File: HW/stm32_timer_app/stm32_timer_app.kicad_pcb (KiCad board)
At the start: 2 copper layers, 142.1 x 79.7 mm, 69 parts, among them J1 105164-0001, J2 61300411121, J3 PH2-06-UA, J4 691213710002, J5 691213710002, Q1 BTA10-600BRG, U1 RT9193-33GB, U2 MOC3041SM, U3 STM32F103C8T6, Y1 ABL-8.000MHZ-B2, Y2 ABS25-32.768KHZ-6-4-T

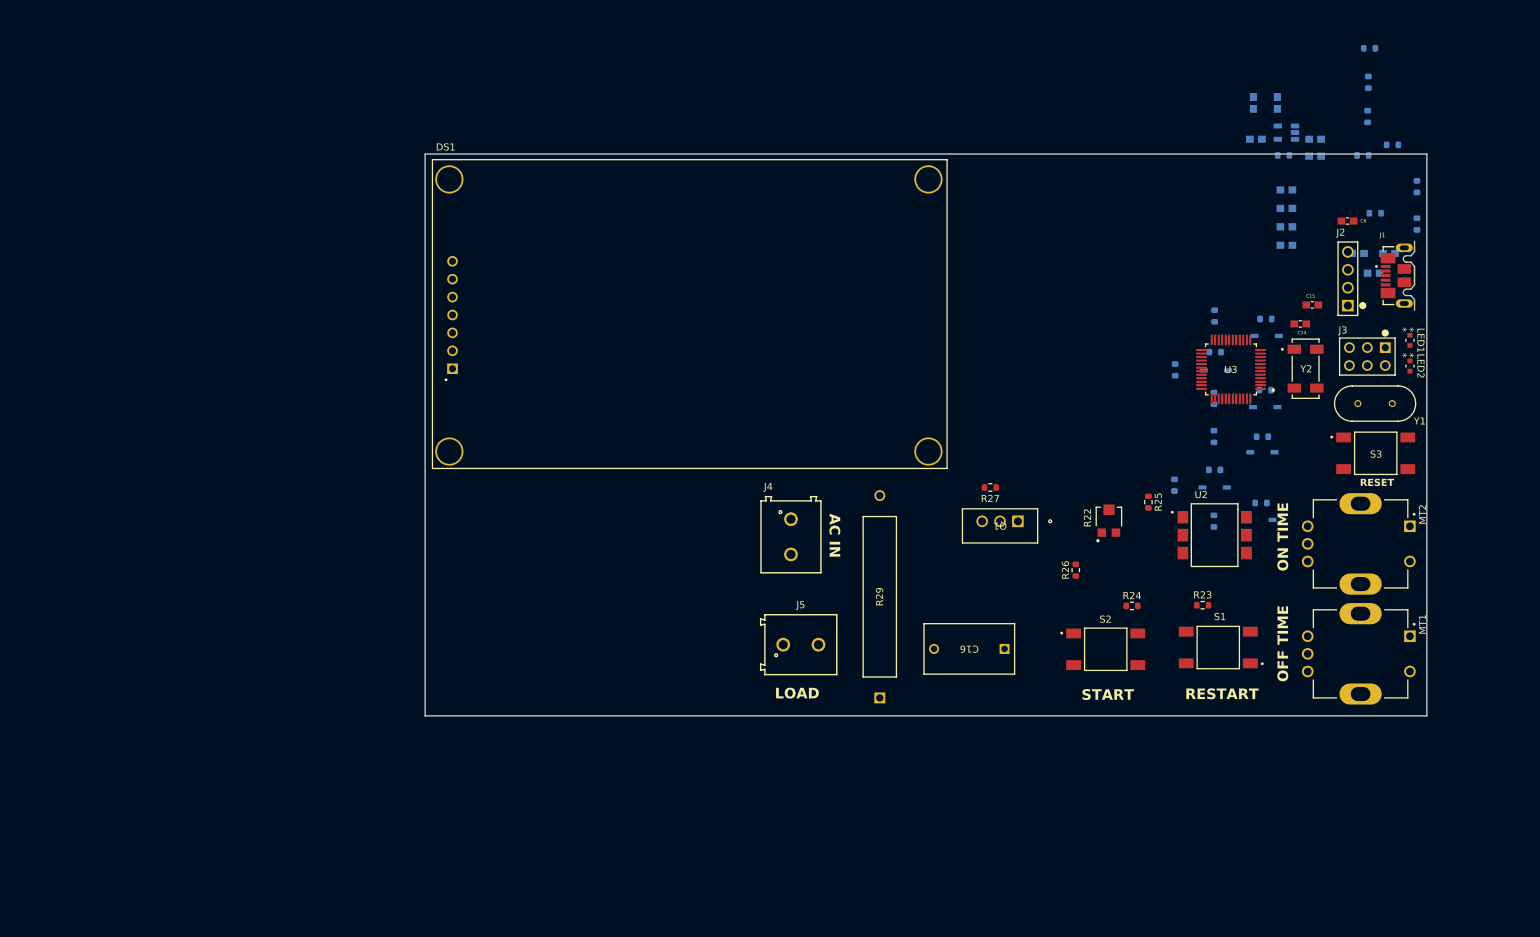
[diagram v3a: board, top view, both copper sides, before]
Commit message: update schematic
update schematic and foot print / 3D body libraries
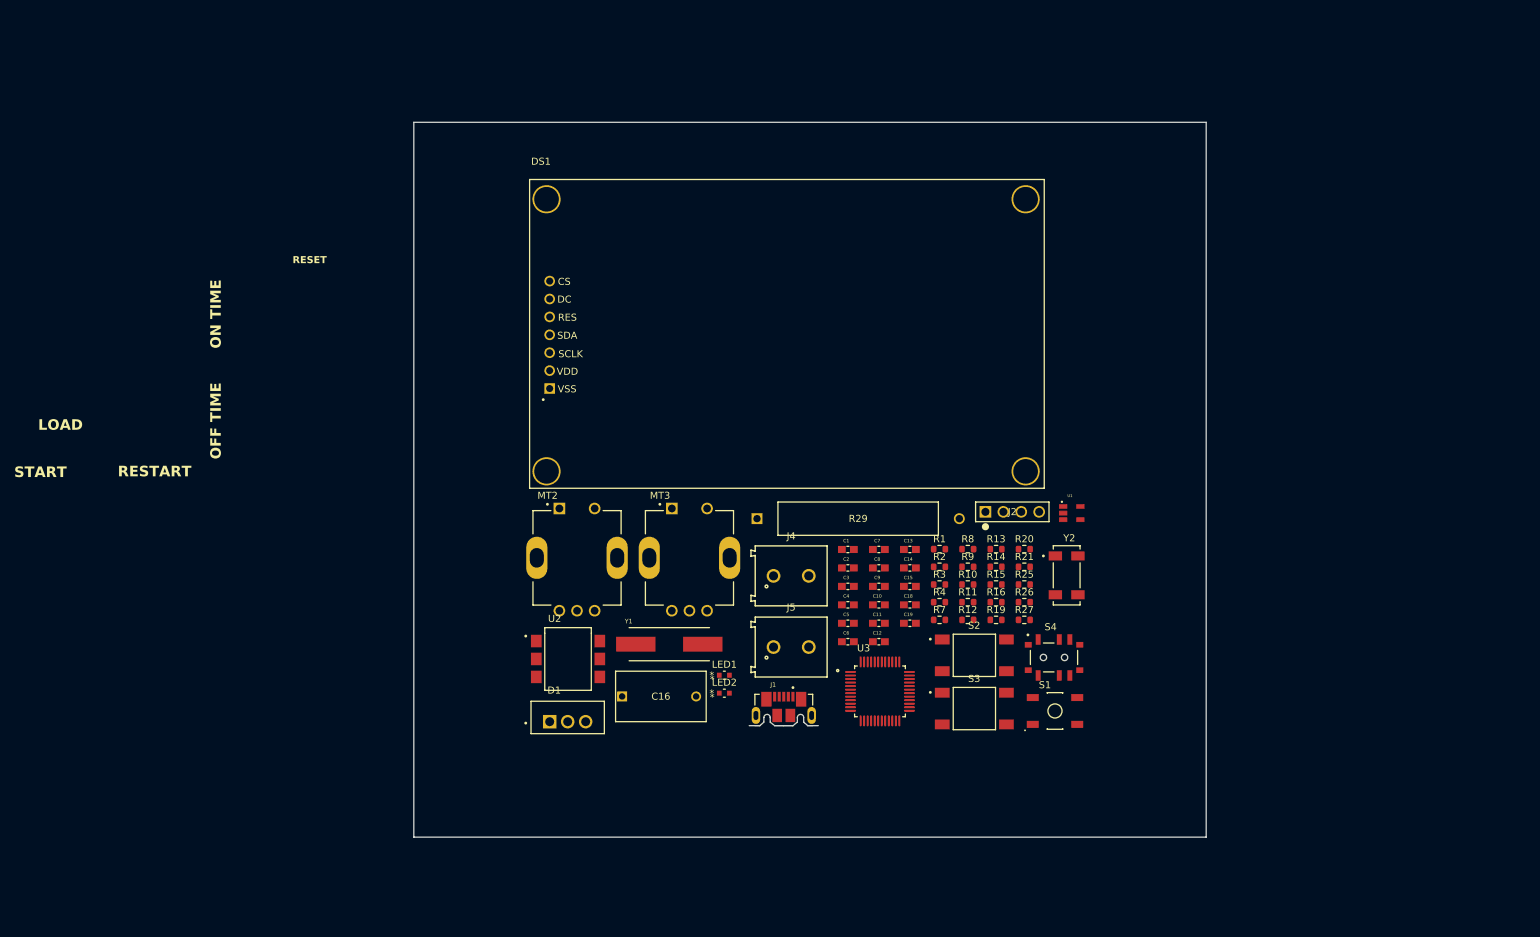
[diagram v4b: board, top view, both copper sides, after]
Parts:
- removed CR1, CR2, CR3, CR4, CR5, CR6: 1N4148W-13-F, 1N4148W_13_F:SOD123_DIO
- removed J3: PH2-06-UA, PH2_06_UA:CONN_PH2-06-UA_ADM
- removed MT1: PEC11R-4215F-S0024, PEC11R-4215F-S0024:XDCR_PEC11R-4215F-S0024
- removed Q1: BTA10-600BRG, BTA10_600BRG:TO-220AB_STM
- removed R17, R18: 10K, Resistor_SMD:R_0603_1608Metric
- removed R22: TC33X-2-102E, TC33X_2_102E:TRIM_TC33X-2-102E
- removed R23, R24: 220, Resistor_SMD:R_0603_1608Metric
- removed R5, R6: 100K, Resistor_SMD:R_0603_1608Metric
- added C18: 105, LD03ZD475MAB2A:CAPC1608X90, F.Cu at (185.6, 101.7)
- added C19: 105, LD03ZD475MAB2A:CAPC1608X90, F.Cu at (185.6, 104.4)
- added D1: BTA16-600B, BTA16-600B:TO255P1040X460X1975-3, F.Cu at (134.5, 118.3)
- added MT3: PEC11R-4215F-S0024, PEC11R-4215F-S0024:XDCR_PEC11R-4215F-S0024, F.Cu at (154.3, 95.1)
- added S4: MSS6-V-T_R, MSS6-V-T_R:SW_MSS6-V-T_R, F.Cu at (206.0, 109.2)
- C1, C10, C11, C12, C13, C2, C3, C4, C5, C7, C8, C9, R1, R13, R14, R15, R19, R2, R20, R21, R3, R9, U1: moved to F.Cu
- R10, R16: value 10K -> 100K; moved to F.Cu
- R11, R12, R4: value 10K -> 330; moved to F.Cu
- R7, R8: value 100K -> 330; moved to F.Cu
- S1: value 1571527-1 -> TL3342F160QG; footprint 1571527-1:SW_1571527-1 -> TL3342F160QG:SW_TL3342F160QG
- Y1: value ABL-8.000MHZ-B2 -> ABLS-8.000MHZ-B2-T; footprint ABL-8.000MHZ-B2:XTAL_HC49P488W46L1150T500H350 -> ABLS-8.000MHZ-B2-T:XTAL_ABLS-8.000MHZ-B2-T
- moved MT2 111.2 mm to (138.4, 95.1), turned to 0 degrees
- moved J1 109.9 mm to (167.7, 118.9), turned to 0 degrees
- moved LED1 108.2 mm to (159.3, 111.7), turned to 0 degrees
- moved LED2 107.8 mm to (159.3, 114.3), turned to 0 degrees
- moved Y1 105.8 mm to (151.4, 107.3)
- moved R3 97.5 mm to (189.8, 98.9), turned to 0 degrees
- moved C4 93.7 mm to (176.8, 101.7), turned to 0 degrees
- moved C5 93.6 mm to (176.8, 104.4), turned to 0 degrees
- moved U2 93.4 mm to (137.1, 109.4)
- moved R7 93.1 mm to (189.8, 103.9)
- moved C6 92.7 mm to (176.8, 107.0)
- moved R2 91.8 mm to (189.8, 96.4), turned to 0 degrees
- moved C2 88.3 mm to (176.8, 96.5), turned to 0 degrees
- moved C1 88.2 mm to (176.8, 93.9), turned to 0 degrees
- moved C12 87.5 mm to (181.2, 107.0), turned to 0 degrees
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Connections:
- C10 pad 1: Net-(C10-Pad1) -> +3.3V
- C10 pad 2: PA3 -> Net-(C10-Pad2)
- C11 pad 1: Net-(C10-Pad1) -> +3.3V
- C11 pad 2: PA3 -> Net-(C10-Pad2)
- C15 pad 1: Net-(C14-Pad1) -> Net-(C15-Pad1)
- C2 pad 1: Net-(C1-Pad1) -> Net-(C2-Pad1)
- C4 pad 2: PA3 -> +3.3V
- C5 pad 2: PA3 -> +3.3V
- C6 pad 1: PA3 -> +3.3V
- C8 pad 1: Net-(C10-Pad1) -> +3.3V
- C8 pad 2: PA3 -> Net-(C10-Pad2)
- C9 pad 1: Net-(C10-Pad1) -> +3.3V
- C9 pad 2: PA3 -> Net-(C10-Pad2)
- J2 pad 1: PA3 -> +3.3V
- LED1 pad 2: PA3 -> +3.3V
- LED2 pad 2: PA3 -> +3.3V
- MT2 pad 2: Net-(CR4-Pad2) -> PA2
- MT2 pad A: Net-(CR5-Pad2) -> PA0
- MT2 pad B: Net-(CR6-Pad2) -> PA1
- R10 pad 1: Net-(CR1-Pad2) -> BOOT1
- R10 pad 2: PA5 -> Net-(R10-Pad2)
- R11 pad 1: Net-(CR2-Pad2) -> PA4
- R11 pad 2: PA6 -> +3.3V
- R12 pad 1: Net-(CR3-Pad2) -> PA3
- R12 pad 2: PA7 -> +3.3V
- R13 pad 1: Net-(CR5-Pad2) -> PA2
- R13 pad 2: PA0 -> +3.3V
- R14 pad 1: Net-(CR4-Pad2) -> PA0
- R14 pad 2: PA2 -> +3.3V
- R15 pad 1: Net-(CR6-Pad2) -> PA1
- R15 pad 2: PA1 -> +3.3V
- R16 pad 1: Net-(CR1-Pad2) -> Net-(R16-Pad1)
- R16 pad 2: PA3 -> BOOT0
- R19 pad 1: Net-(CR4-Pad2) -> PA2
- R19 pad 2: PA3 -> +3.3V
- R20 pad 1: Net-(CR5-Pad2) -> PA0
- R20 pad 2: PA3 -> +3.3V
- R21 pad 1: Net-(CR6-Pad2) -> PA1
- R21 pad 2: PA3 -> +3.3V
- R4 pad 2: PA3 -> +3.3V
- S1 pad 1: Net-(R23-Pad2) -> unconnected-(S1-Pad1)
- S1 pad 2: Net-(R23-Pad2) -> Net-(S1-Pad2)
- S1 pad 3: PA3 -> unconnected-(S1-Pad3)
- S1 pad 4: PA3 -> RESET
- S2 pad 1: Net-(R24-Pad2) -> Net-(S2-Pad1)
- S2 pad 2: Net-(R24-Pad2) -> PA3
- S2 pad 3: PA3 -> Net-(S2-Pad1)
- S3 pad 1: Net-(C7-Pad2) -> Net-(S3-Pad1)
- S3 pad 2: RESET -> PA4
- S3 pad 3: Net-(C7-Pad2) -> Net-(S3-Pad1)
- S3 pad 4: RESET -> PA4
- U1 pad 5: PA3 -> +3.3V
- U3 pad 14: PA3 -> PA4
- U3 pad 24: PA3 -> +3.3V
- U3 pad 36: PA3 -> +3.3V
- U3 pad 48: PA3 -> +3.3V
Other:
- board size 142.1 x 79.7 mm -> 112.4 x 101.4 mm
- board text removed: "AC IN"

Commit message: update
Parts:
- added J3: 61300411121, 61300411121:CONN_61300411121_WRE, F.Cu at (139.2, 95.5)
- added LS1: AI-1027-TWT-3V-R, AI-1027-TWT-3V-R:XDCR_AI-1027-TWT-3V-R, F.Cu at (224.2, 95.9)
- added U4: MAX31865 AMPLIFIER, MAX31865:MAX31865, F.Cu at (235.7, 69.0)
- added U5: MMBT2222A-7-F, MMBT2222A-7-F:SOT103P240X110-3N, F.Cu at (215.1, 95.8)
- R25, R26, R27, U1: moved to B.Cu
- moved MT3 105.2 mm to (258.2, 78.7)
- moved MT2 105.1 mm to (242.2, 78.7)
- moved J1 75.1 mm to (175.5, 44.2), turned to 180 degrees
- moved LED2 70.5 mm to (221.1, 80.4)
- moved C16 70.4 mm to (151.0, 44.6), turned to -90 degrees
- moved J5 66.8 mm to (138.3, 48.3), turned to 90 degrees
- moved S3 65.9 mm to (257.9, 97.7), turned to 180 degrees
- moved R27 63.9 mm to (150.0, 66.5), turned to 180 degrees
- moved Y1 62.1 mm to (198.4, 66.7), turned to 90 degrees
- moved LED1 61.4 mm to (212.2, 80.6)
- moved R26 60.0 mm to (149.8, 71.5), turned to 180 degrees
- moved D1 58.1 mm to (137.3, 60.3)
- moved R25 56.8 mm to (149.9, 75.7)
- moved U3 48.7 mm to (182.3, 65.3)
- moved S2 48.5 mm to (241.9, 97.7), turned to 180 degrees
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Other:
- board size 112.4 x 101.4 mm -> 137.6 x 64.6 mm
- board text removed: "LOAD"
- board text removed: "RESET"

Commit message: schematic
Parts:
- removed the J3 at (139.2, 95.5)
- removed MT3: PEC11R-4215F-S0024, PEC11R-4215F-S0024:XDCR_PEC11R-4215F-S0024
- removed the R10 at (202.0, 95.2)
- removed the R11 at (202.0, 97.7)
- removed the R25 at (149.9, 75.7)
- removed the R26 at (149.8, 71.5)
- removed the R27 at (150.0, 66.5)
- removed the S4 at (222.0, 63.7)
- removed the U4 at (235.7, 69.0)
- added C16: 105, LD03ZD475MAB2A:CAPC1608X90, F.Cu at (211.8, 90.9)
- added C17: 105, LD03ZD475MAB2A:CAPC1608X90, F.Cu at (219.3, 91.0)
- added J4: 61300411121, 61300411121:CONN_61300411121_WRE, F.Cu at (162.7, 99.6)
- added J5: 61300411121, 61300411121:CONN_61300411121_WRE, F.Cu at (176.9, 99.6)
- added J6: 61300411121, 61300411121:CONN_61300411121_WRE, F.Cu at (169.6, 99.6)
- added LED1: 150060GS75000, 150060GS75000:LED_150060GS75000_WRE, F.Cu at (246.8, 86.0)
- added LED2: 150060GS75000, 150060GS75000:LED_150060GS75000_WRE, F.Cu at (243.3, 86.0)
- added LED3: 150060GS75000, 150060GS75000:LED_150060GS75000_WRE, F.Cu at (127.5, 83.6)
- added LED4: 150060GS75000, 150060GS75000:LED_150060GS75000_WRE, F.Cu at (127.5, 77.4)
- added MT1: PEC11R-4215F-S0024, PEC11R-4215F-S0024:XDCR_PEC11R-4215F-S0024, F.Cu at (258.2, 97.2)
- added R19: 100K, Resistor_SMD:R_0603_1608Metric, F.Cu at (235.9, 97.7)
- added R2: 1K, Resistor_SMD:R_0603_1608Metric, F.Cu at (138.7, 85.7)
- added R20: 330, Resistor_SMD:R_0603_1608Metric, F.Cu at (211.6, 89.1)
- added R21: 330, Resistor_SMD:R_0603_1608Metric, F.Cu at (219.2, 89.1)
- added R22: 330, Resistor_SMD:R_0603_1608Metric, F.Cu at (195.2, 102.6)
- added R3: 360, Resistor_SMD:R_0603_1608Metric, F.Cu at (136.4, 61.2)
- added R4: 330, Resistor_SMD:R_0603_1608Metric, F.Cu at (232.8, 120.2)
- added R6: 330, Resistor_SMD:R_0603_1608Metric, F.Cu at (225.9, 78.3)
- added R7: 330, Resistor_SMD:R_0603_1608Metric, F.Cu at (137.1, 66.9)
- added R8: 330, Resistor_SMD:R_0603_1608Metric, F.Cu at (131.1, 83.6)
- added R9: 330, Resistor_SMD:R_0603_1608Metric, F.Cu at (131.1, 77.3)
- added REF**: MountingHole_3.2mm_M3_Pad, MountingHole:MountingHole_3.2mm_M3_Pad, F.Cu at (269.1, 108.4)
- added REF**: MountingHole_3.2mm_M3_Pad, MountingHole:MountingHole_3.2mm_M3_Pad, F.Cu at (157.1, 108.4)
- added REF**: MountingHole_3.2mm_M3_Pad, MountingHole:MountingHole_3.2mm_M3_Pad, F.Cu at (147.5, 108.4)
- added REF**: MountingHole_3.2mm_M3_Pad, MountingHole:MountingHole_3.2mm_M3_Pad, F.Cu at (147.5, 39.9)
- added REF**: MountingHole_3.2mm_M3_Pad, MountingHole:MountingHole_3.2mm_M3_Pad, F.Cu at (115.4, 39.9)
- added REF**: MountingHole_3.2mm_M3_Pad, MountingHole:MountingHole_3.2mm_M3_Pad, F.Cu at (115.4, 108.4)
- added REF**: MountingHole_3.2mm_M3_Pad, MountingHole:MountingHole_3.2mm_M3_Pad, F.Cu at (157.1, 39.9)
- added REF**: MountingHole_3.2mm_M3_Pad, MountingHole:MountingHole_3.2mm_M3_Pad, F.Cu at (269.1, 39.9)
- added S2: 1571527-1, 1571527-1:SW_1571527-1, F.Cu at (203.3, 91.5)
- added S5: 1571527-1, 1571527-1:SW_1571527-1, F.Cu at (203.3, 100.0)
- added S7: MSS-102559-14A-D, MSS-102559-14A-D:SW_MSS-102559-14A-D, F.Cu at (244.9, 99.4)
- added S8: MSS-102559-14A-D, MSS-102559-14A-D:SW_MSS-102559-14A-D, F.Cu at (239.2, 99.4)
- added U2: STM32F103C8T6, STM32F103C8T6:QFP50P900X900X160-48N, B.Cu at (184.6, 53.9)
- C10: renamed from C3; moved to B.Cu
- C11: renamed from C4; moved to B.Cu
- C12: renamed from C5; moved to B.Cu
- C13: renamed from C1; moved to B.Cu
- C14: renamed from C2; moved to B.Cu
- C20: renamed from C6; moved to B.Cu
- R12: renamed from R15; moved to B.Cu
- R13: renamed from R14; moved to B.Cu
- R14: renamed from R13; moved to B.Cu
- R15: renamed from R21; moved to B.Cu
- R16: renamed from R20; moved to B.Cu
- R17: renamed from R19; moved to B.Cu
- R18: renamed from R16; moved to B.Cu
- R27: renamed from R3; moved to B.Cu
- U3: value STM32F103C8T6 -> MAX31865 AMPLIFIER; footprint STM32F103C8T6:QFP50P900X900X160-48N -> MAX31865:MAX31865
- U5: moved to B.Cu
- Y1: value ABLS-8.000MHZ-B2-T -> ABM3-8.000MHZ-J4Q-T; footprint ABLS-8.000MHZ-B2-T:XTAL_ABLS-8.000MHZ-B2-T -> ABM3_8_000MHZ_J4Q_T:XTAL_ABM3-8.000MHZ-J4Q-T; moved to B.Cu
- Y2: value ABS25-32.768KHZ-6-4-T -> ABS07-32.768KHZ-T; footprint ABS25-32.768KHZ-6-4-T:XTAL_ABS25-32.768KHZ-6-4-T -> ABS07-32.768KHZ-T:XTAL_ABS07-32.768KHZ-T; moved to B.Cu
- moved C7 61.9 mm to (247.4, 126.5)
- moved C8 61.9 mm to (247.4, 123.9)
- moved C1 61.9 mm to (247.4, 121.3)
- moved R1 61.9 mm to (255.6, 123.7)
- moved C3 61.9 mm to (243.0, 123.9)
- moved C4 61.9 mm to (243.0, 126.5)
- moved C9 61.9 mm to (243.0, 131.8)
- moved C2 61.9 mm to (243.0, 134.4)
- moved C6 61.9 mm to (243.0, 129.1)
- moved C12 56.3 mm to (174.4, 45.4), turned to -90 degrees
- moved C11 55.6 mm to (170.3, 44.4)
- moved U3 54.1 mm to (236.3, 69.0)
- moved R26 53.9 mm to (162.5, 52.2), turned to -90 degrees
- moved R25 53.5 mm to (163.3, 49.5)
- moved R27 51.9 mm to (167.8, 52.9), turned to -90 degrees
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- renumbered C13 to C1, C7 to C15, C12 to C2, C8 to C3, C9 to C4, C16 to C5, C10 to C6, C15 to C7, C14 to C8, C11 to C9, J4 to J1, J5 to J3, J1 to J7, LED1 to LED5, LED2 to LED6, R9 to R1, R7 to R10, R8 to R11, R12 to R23, R4 to R24, R1 to R25, R2 to R26, R29 to R5, S1 to S4, S2 to S6, U2 to U1, U1 to U4
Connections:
- net +5V renamed /+5V
- C1 pad 2: OSCOUT -> /OSCOUT
- C11 pad 2: +3.3V -> /+3.3V
- C12 pad 2: +3.3V -> /+3.3V
- C15 pad 1: RESET -> /RESET
- C18 pad 1: PA4 -> /PA4
- C19 pad 1: PA3 -> /PA3
- C2 pad 2: OSCIN -> /OSCIN
- C20 pad 1: +3.3V -> /+3.3V
- C20 pad 2: Net-(C6-Pad2) -> Net-(C20-Pad2)
- C3 pad 1: +3.3V -> /+3.3V
- C4 pad 1: +3.3V -> /+3.3V
- C6 pad 1: +3.3V -> /+3.3V
- C7 pad 2: PC15 -> /PC15
- C8 pad 2: PC14 -> /PC14
- C9 pad 1: +3.3V -> /+3.3V
- DS1 pad 1: unconnected-(DS1-GND-Pad1) -> Net-(DS1-GND)
- DS1 pad 2: unconnected-(DS1-VDD-Pad2) -> /+3.3V
- DS1 pad 3: unconnected-(DS1-SCL-Pad3) -> /PA5
- DS1 pad 4: unconnected-(DS1-SDA-Pad4) -> /PA7
- DS1 pad 5: unconnected-(DS1-RST-Pad5) -> /PA6
- DS1 pad 6: unconnected-(DS1-DC-Pad6) -> /PB3
- DS1 pad 7: unconnected-(DS1-CS-Pad7) -> /PB6
- J2 pad 1: +3.3V -> /+3.3VT
- J2 pad 2: SWDIO -> Net-(J2-Pad2)
- J2 pad 3: SWDCLK -> /PA10T
- J2 pad 4: Net-(C6-Pad2) -> Net-(J2-Pad4)
- LED5 pad 2: +3.3V -> /+3.3V
- LED6 pad 2: +3.3V -> /+3.3V
- LS1 pad N: unconnected-(LS1-PadN) -> Net-(U5-C)
- LS1 pad P: unconnected-(LS1-PadP) -> /+3.3V
- MT2 pad 2: PA2 -> /PB0
- MT2 pad A: PA0 -> /PB5
- MT2 pad B: PA1 -> /PB4
- R1 pad 1: OSCIN -> /OSCIN
- R1 pad 2: OSCOUT -> /OSCOUT
- R10 pad 1: PC13 -> /PC13
- R12 pad 1: PA1 -> /PA1
- R12 pad 2: +3.3V -> /+3.3V
- R13 pad 1: PA0 -> /PA0
- R13 pad 2: +3.3V -> /+3.3V
- R14 pad 1: PA2 -> /PA2
- R14 pad 2: +3.3V -> /+3.3V
- R15 pad 1: PA1 -> /PB4
- R15 pad 2: +3.3V -> /+3.3V
- R16 pad 1: PA0 -> /PB5
- R16 pad 2: +3.3V -> /+3.3V
- R17 pad 1: PA2 -> /PB0
- R17 pad 2: +3.3V -> /+3.3V
- R18 pad 2: BOOT0 -> /BOOT0
- R23 pad 1: PA3 -> /PA3
- R23 pad 2: +3.3V -> /+3.3V
- R24 pad 1: RESET -> /RESET
- R24 pad 2: +3.3V -> /+3.3V
- R25 pad 2: PA11 -> /PA11
- R26 pad 2: PA12 -> /PA12
- R27 pad 2: PA12 -> /PA12
- S3 pad 2: PA4 -> /PA9
- S3 pad 4: PA4 -> /PA9
- S4 pad 4: RESET -> /RESET
- S6 pad 2: PA3 -> /PA3
- S6 pad 4: PA3 -> /PA3
- U3 pad 1: unconnected-(U3-VBAT-Pad1) -> /+3.3V
- U3 pad 10: PA0 -> unconnected-(U3-RTD--Pad10)
- U3 pad 11: PA1 -> unconnected-(U3-RTD+-Pad11)
- U3 pad 12: PA2 -> unconnected-(U3-F+-Pad12)
- U3 pad 2: PC13 -> Net-(U3-GND)
- U3 pad 3: PC14 -> unconnected-(U3-3V3-Pad3)
- U3 pad 4: PC15 -> /PB13
- U3 pad 5: OSCIN -> /PB15
- U3 pad 6: OSCOUT -> /PB14
- U3 pad 7: RESET -> /PB12
- U3 pad 8: unconnected-(U3-VSSA-Pad8) -> /PB11
- U4 pad 5: +3.3V -> /+3.3V
- U5 pad 1: unconnected-(U5-B-Pad1) -> /PB1
- U5 pad 2: unconnected-(U5-E-Pad2) -> Net-(U5-E)
- U5 pad 3: unconnected-(U5-C-Pad3) -> Net-(U5-C)
- Y1 pad 1: OSCIN -> /OSCIN
- Y1 pad 2: OSCOUT -> /OSCOUT
- Y2 pad 1: PC14 -> /PC14
- Y2 pad 2: unconnected-(Y2-NC-Pad2) -> /PC15
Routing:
- net /+3.3V: track 0.00 -> 224.9 mm, vias 0 -> 1
- net /PB0: track 0.00 -> 121.7 mm
- net /PA2: track 0.00 -> 98.2 mm, vias 0 -> 1
- net /PB4: track 0.00 -> 92.9 mm, vias 0 -> 1
- net /PB5: track 0.00 -> 90.4 mm, vias 0 -> 1
- net /PA1: track 0.00 -> 90.0 mm, vias 0 -> 1
- net /PA0: track 0.00 -> 85.2 mm, vias 0 -> 1
- net /BOOT0: track 0.00 -> 73.8 mm
- net /PA3: track 0.00 -> 71.4 mm, vias 0 -> 1
- net /PA9: track 0.00 -> 70.4 mm, vias 0 -> 1
- net /PA8: track 0.00 -> 64.8 mm, vias 0 -> 1
- net /PA15: track 0.00 -> 58.3 mm, vias 0 -> 2
- net /SWDIO: track 0.00 -> 54.4 mm, vias 0 -> 1
- net /PB7: track 0.00 -> 53.7 mm, vias 0 -> 1
- net /PA10: track 0.00 -> 53.1 mm, vias 0 -> 1
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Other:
- board size 137.6 x 64.6 mm -> 161.3 x 76.1 mm
- board text added: "AC IN"
- board text added: "AC OUT"
- board text added: "BOOT0"
- board text added: "BOOT1"
- board text added: "Button1"
- board text added: "Button2"
- board text added: "PINs"
- board text added: "RESET"
- board text added: "ST-Link"
- board text added: "TEMP SENSOR"
- board text added: "TRIAC"
- board text added: "TRIAC DRIVER"

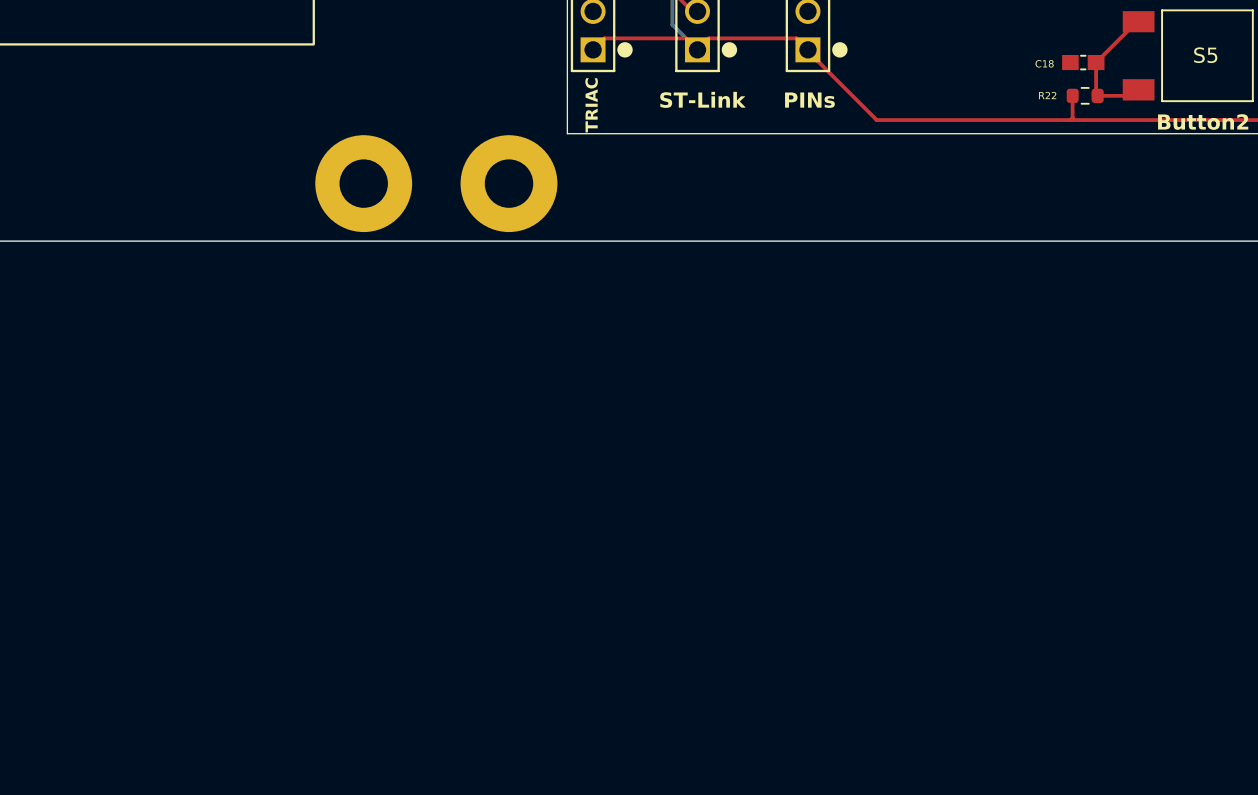
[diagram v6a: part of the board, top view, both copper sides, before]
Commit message: schematic update
mcu changed
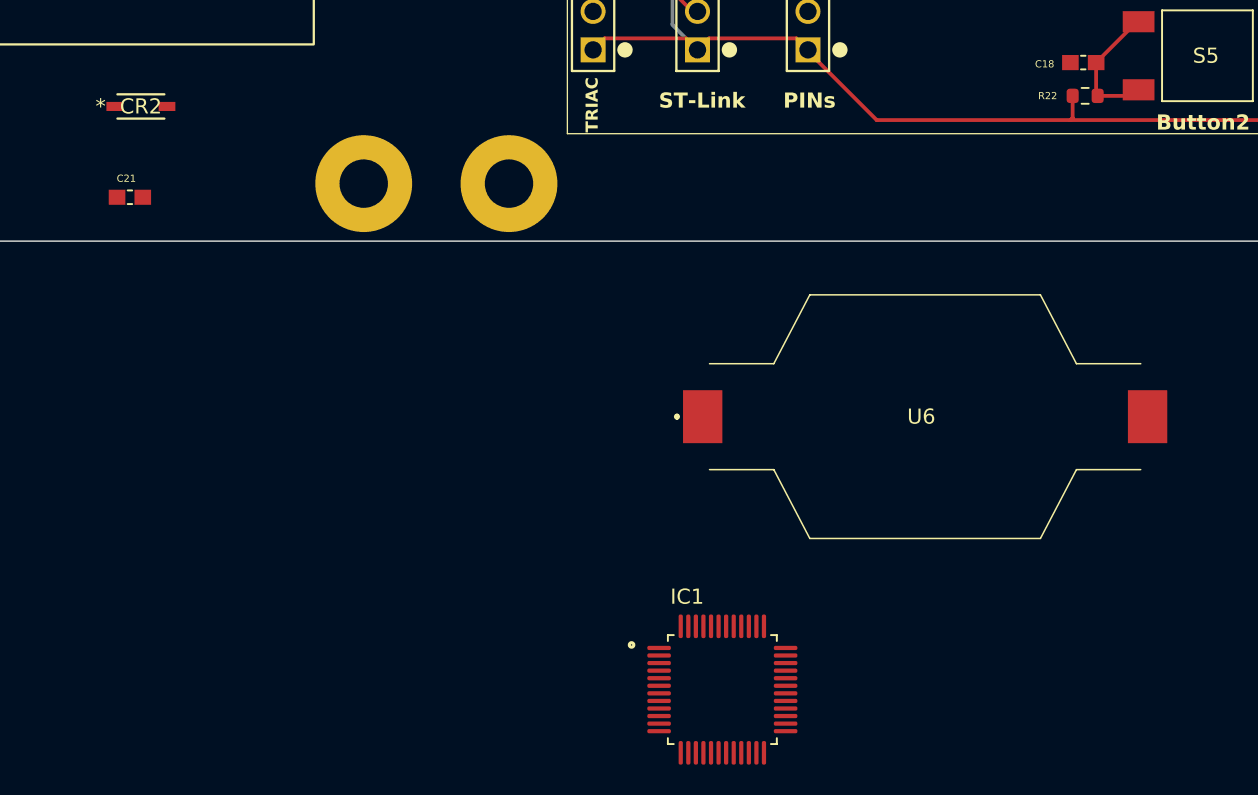
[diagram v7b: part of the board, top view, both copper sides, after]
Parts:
- added C21: LD03ZD475MAB2A, LD03ZD475MAB2A:CAPC1608X90, F.Cu at (132.1, 109.3)
- added CR2: 1N4148W-13-F, 1N4148W_13_F:SOD123_DIO, F.Cu at (132.8, 103.3)
- added IC1: STM32F303C8T6, STM32F103C8T6:QFP50P900X900X160-48N, F.Cu at (171.2, 141.8)
- added U6: SMTU2032-LF, SMTU2032-LF:SMTU2032LF, F.Cu at (184.6, 123.8)
